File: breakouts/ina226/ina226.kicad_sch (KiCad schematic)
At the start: 14 parts, among them J1 Conn_01x01_Pin, J2 Conn_01x01_Pin, J3 Conn_01x01_Pin, J4 Conn_01x01_Pin, J5 Conn_01x01_Pin, J6 Conn_01x01_Pin, J7 Conn_01x01_Pin, J8 Conn_01x01_Pin, U1 INA226

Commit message: Feat[breakouts]: Added @TODOs
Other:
- note added: "@TODO: Add at least 1 more peripheral address config"
- note added: "@TODO: Add screw terminal for Vin+ and Vin-"
- note added: "@TODO: Assign footprints"
- note added: "@TODO: Change VS voltage"
- note added: "@TODO: Don't short the entire thing (use labels for vin+ and vin-)"
- note added: "@TODO: Fix styling (Use default symbols for voltage, ground must face ground)"
- note added: "@TODO: Remove header pins for Vin+, Vin-, A0, A1"
- note added: "@TODO: Remove series resistors"
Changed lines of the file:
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@@
-(kicad_sch (version 20230121) (generator eeschema)
+(kicad_sch (version 20230409) (generator eeschema)
   (paper "A4")
   (title_block
@@
     (fill (type none))
   )
-  (text "Chip" (at 194.31 67.31 0)
+  (text "Chip" (exclude_from_sim no)
+ (at 194.31 67.31 0)
     (effects (font (size 1.27 1.27)) (justify left bottom))
   )
-  (text "Header" (at 171.45 21.59 0)
+  (text "@TODO: Add at least 1 more peripheral address config" (exclude_from_sim no)
+    (at 23.241 97.028 0)
     (effects (font (size 1.27 1.27)) (justify left bottom))
   )
+  (text "@TODO: Remove series resistors" (exclude_from_sim no)
+ (at 23.368 82.55 0)
+    (effects (font (size 1.27 1.27)) (justify left bottom))
+  )
+  (text "@TODO: Don't short the entire thing (use labels for vin+ and vin-)" (exclude_from_sim no)
+    (at 23.241 77.597 0)
+    (effects (font (size 1.27 1.27)) (justify left bottom))
+  )
+  (text "@TODO: Remove header pins for Vin+, Vin-, A0, A1" (exclude_from_sim no)
+ (at 23.241 101.854 0)
+    (effects (font (size 1.27 1.27)) (justify left bottom))
+  )
+  (text "@TODO: Change VS voltage" (exclude_from_sim no)
+ (at 23.495 73.025 0)
+    (effects (font (size 1.27 1.27)) (justify left bottom))
+  )
+  (text "@TODO: Add screw terminal for Vin+ and Vin-\n" (exclude_from_sim no)
+ (at 23.241 87.63 0)
+    (effects (font (size 1.27 1.27)) (justify left bottom))
+  )
+  (text "Header" (exclude_from_sim no)
+ (at 171.45 21.59 0)
+    (effects (font (size 1.27 1.27)) (justify left bottom))
+  )
+  (text "@TODO: Fix styling (Use default symbols for voltage, ground must face ground)" (exclude_from_sim no)
+    (at 23.114 92.202 0)
+    (effects (font (size 1.27 1.27)) (justify left bottom))
+  )
+  (text "@TODO: Assign footprints" (exclude_from_sim no)
+ (at 22.86 107.188 0)
+    (effects (font (size 1.27 1.27)) (justify left bottom))
+  )

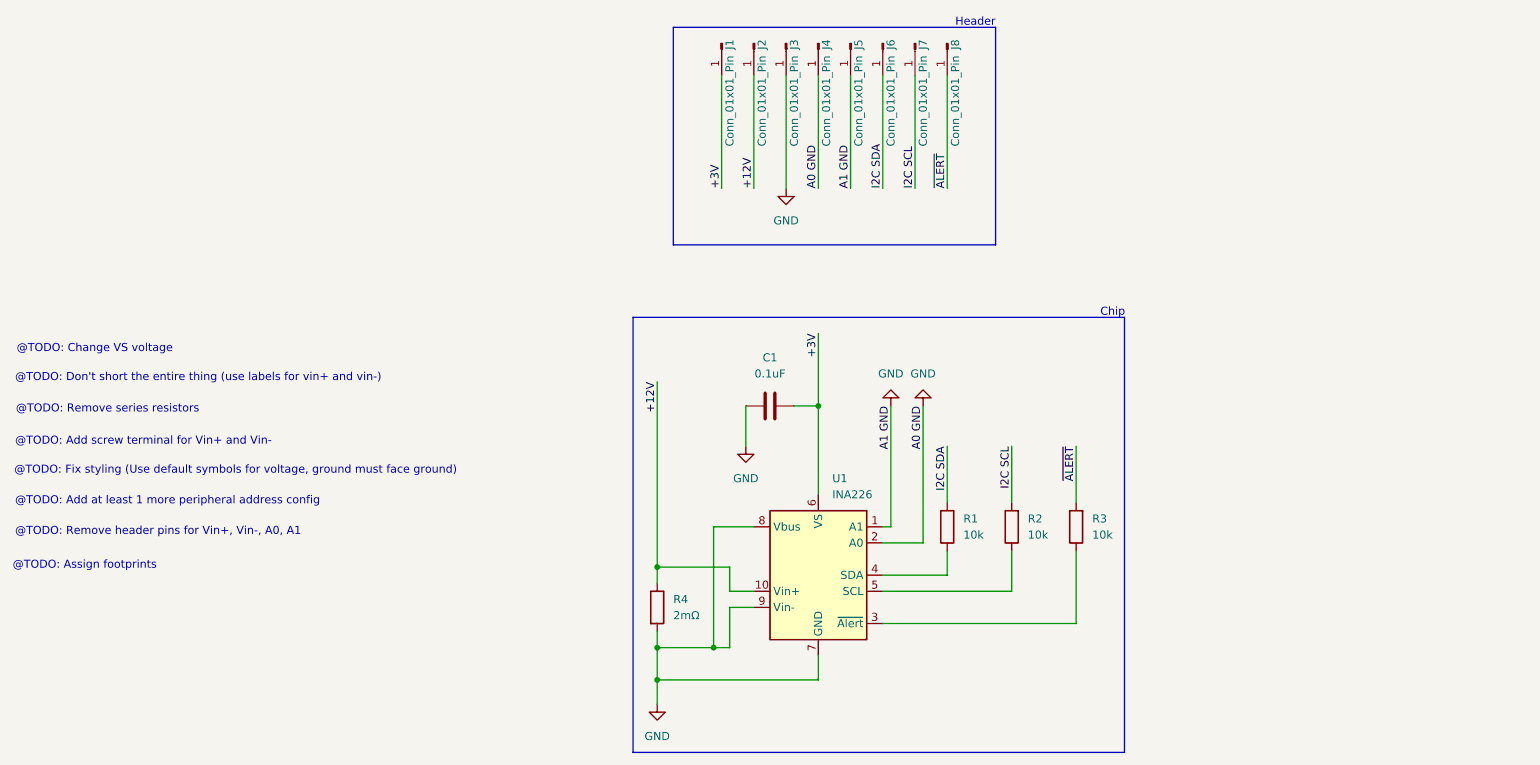
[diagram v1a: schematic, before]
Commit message: Feat[breakouts]: Fixed listed problems with ina226 breakout
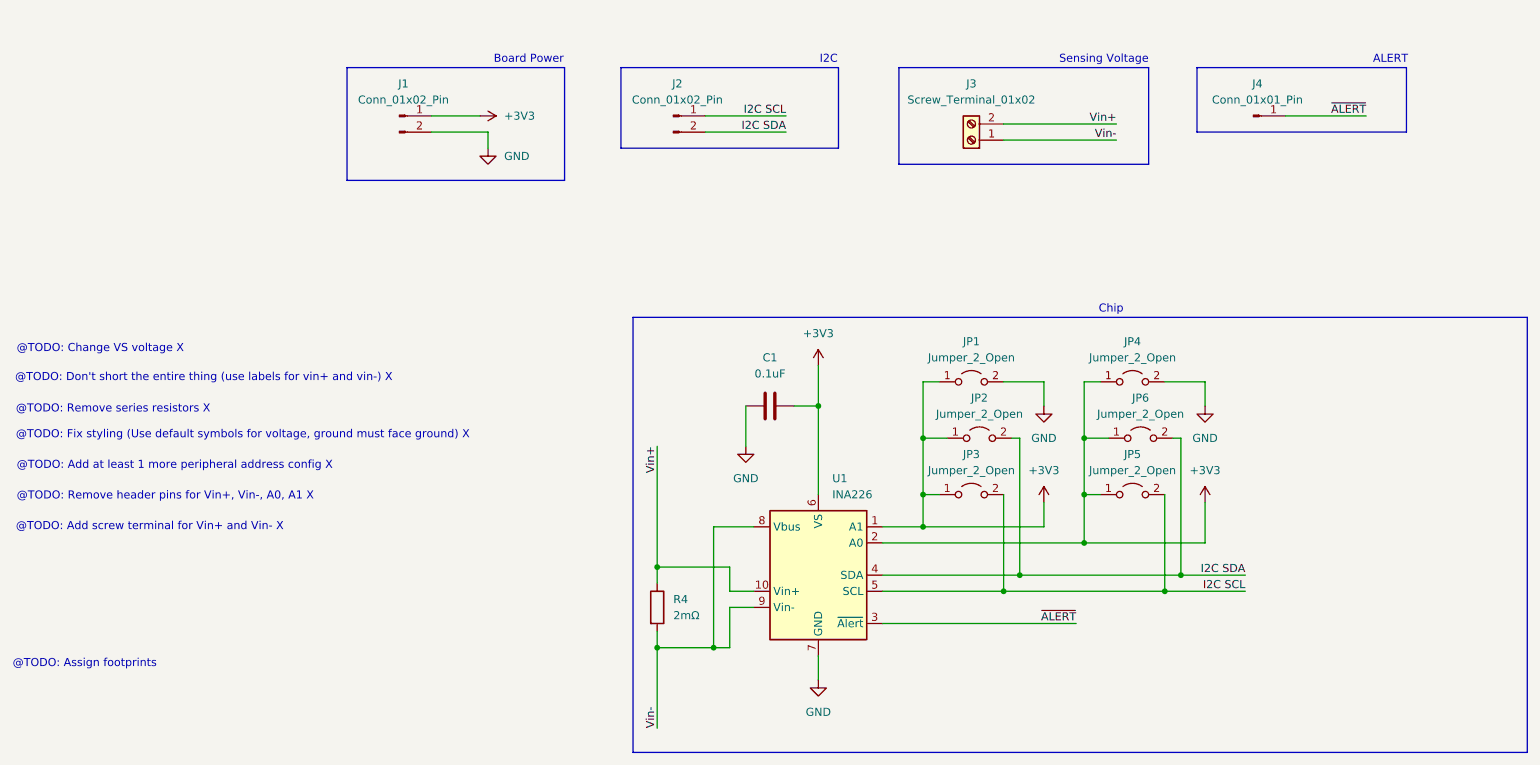
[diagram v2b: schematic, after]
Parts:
- removed J1, J2, J3, J5, J6, J7, J8: Conn_01x01_Pin, symbol Connector:Conn_01x01_Pin
- removed R1, R2, R3: 10k, symbol Device:R
- added J1, J2: Conn_01x02_Pin, symbol Connector:Conn_01x02_Pin
- added J3: Screw_Terminal_01x02, symbol Connector:Screw_Terminal_01x02
- added JP1, JP2, JP3, JP4, JP5, JP6: Jumper_2_Open, symbol Jumper:Jumper_2_Open
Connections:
- net GND: now also J1.2 (Pin_2), JP1.2 (B), JP4.2 (B); no longer J4.1 (Pin_1), R4.2, U1.1 (A1), U1.2 (A0), U1.8 (Vbus), U1.9 (Vin-)
- net I2C SCL: now also U1.5 (SCL), J2.1 (Pin_1), JP3.2 (B), JP5.2 (B)
- net I2C SDA: now also U1.4 (SDA), J2.2 (Pin_2), JP2.2 (B), JP6.2 (B)
- net ~{ALERT}: now also J4.1 (Pin_1), U1.3 (~{Alert})
- net +12V renamed Vin+
- net Vin+: now also J3.2 (Pin_2)
- net +3V renamed +3V3
- net +3V3: now also U1.1 (A1), U1.2 (A0), J1.1 (Pin_1), JP1.1 (A), JP2.1 (A), JP3.1 (A), JP4.1 (A), JP5.1 (A), JP6.1 (A)
- new net Vin-: J3.1 (Pin_1), R4.2, U1.8 (Vbus), U1.9 (Vin-)
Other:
- note added: "@TODO: Add at least 1 more peripheral address config X"
- note added: "@TODO: Add screw terminal for Vin+ and Vin- X"
- note added: "@TODO: Change VS voltage X"
- note added: "@TODO: Don't short the entire thing (use labels for vin+ and vin-) X"
- note added: "@TODO: Fix styling (Use default symbols for voltage, ground must face ground) X"
- note added: "@TODO: Remove header pins for Vin+, Vin-, A0, A1 X"
- note added: "@TODO: Remove series resistors X"
- note added: "ALERT"
- note added: "Board Power"
- note added: "I2C"
- note added: "Sensing Voltage"
- note removed: "@TODO: Add at least 1 more peripheral address config"
- note removed: "@TODO: Add screw terminal for Vin+ and Vin-"
- note removed: "@TODO: Change VS voltage"
- note removed: "@TODO: Don't short the entire thing (use labels for vin+ and vin-)"
- note removed: "@TODO: Fix styling (Use default symbols for voltage, ground must face ground)"
- note removed: "@TODO: Remove header pins for Vin+, Vin-, A0, A1"
- note removed: "@TODO: Remove series resistors"
- note removed: "Header"

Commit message: Feat[breakouts]: Separated A1/A0 from main chip schem
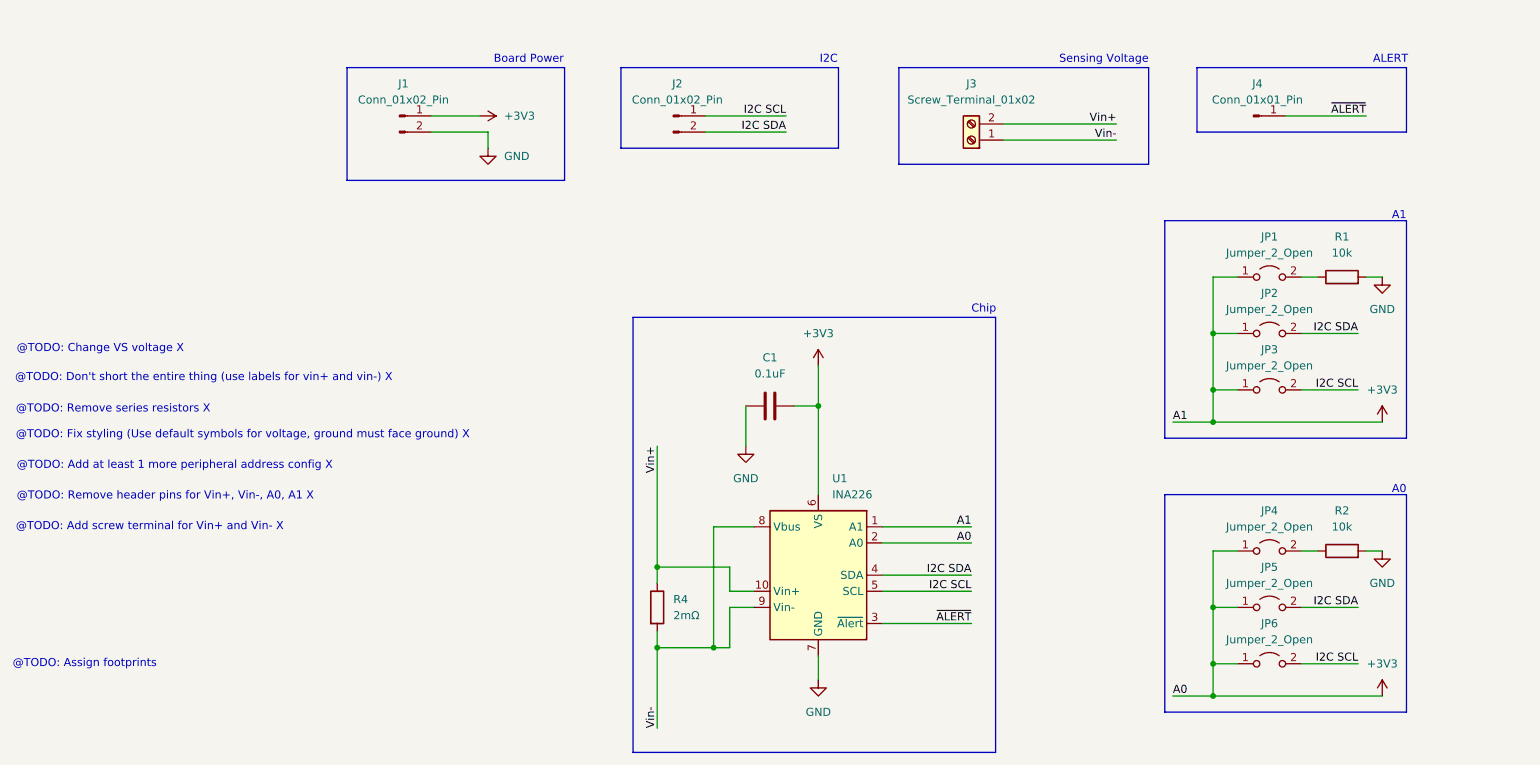
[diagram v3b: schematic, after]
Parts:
- added R1, R2: 10k, symbol Device:R
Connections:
- net GND: now also R1.2, R2.2; no longer JP1.2 (B), JP4.2 (B)
- net I2C SCL: now also JP6.2 (B); no longer JP5.2 (B)
- net I2C SDA: now also JP5.2 (B); no longer JP6.2 (B)
- new net: JP4.2 (B), R2.1
- new net: JP1.2 (B), R1.1
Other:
- note added: "A0"
- note added: "A1"

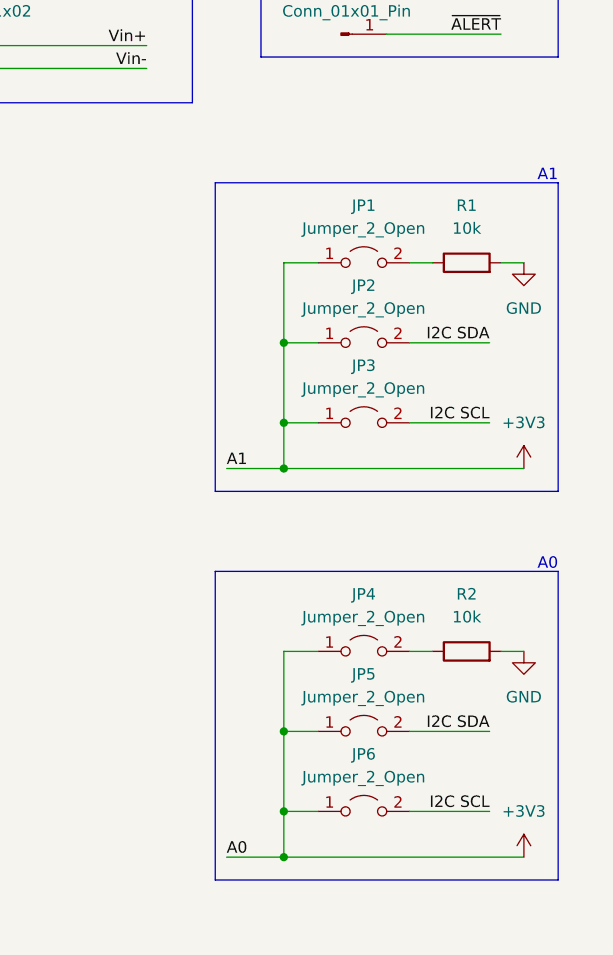
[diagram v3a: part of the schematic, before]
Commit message: Feat[breakouts]: Assigned footprints for INA226
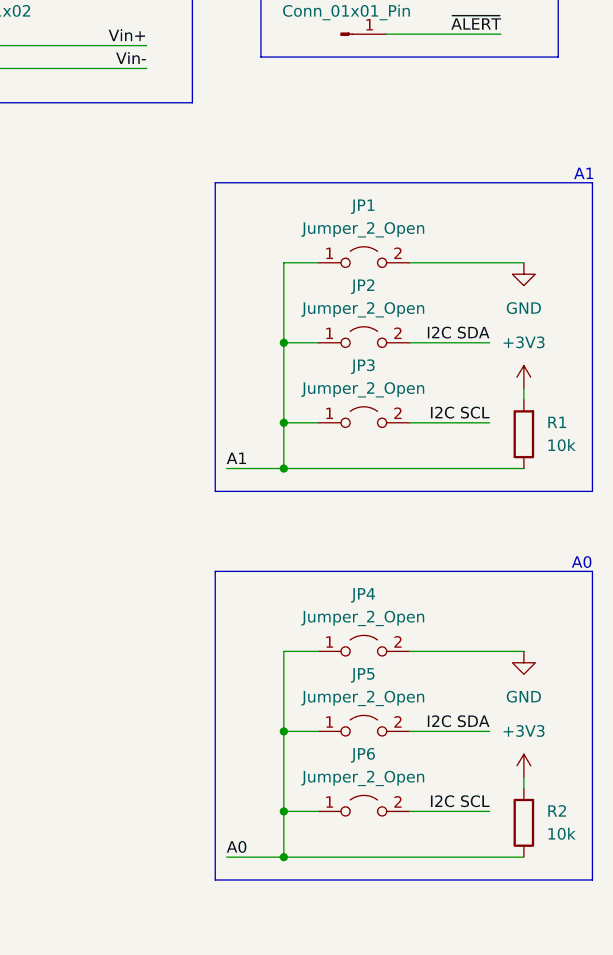
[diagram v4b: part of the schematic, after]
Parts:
- C1: footprint (none) -> Capacitor_SMD:C_0603_1608Metric
- J1, J2: footprint (none) -> Connector_PinSocket_2.54mm:PinSocket_1x02_P2.54mm_Vertical
- J3: footprint (none) -> Conn_1935776:CONN_1935776_PXC
- J4: footprint (none) -> Connector_PinSocket_2.54mm:PinSocket_1x01_P2.54mm_Vertical
- JP1, JP2, JP3, JP4, JP5, JP6: footprint (none) -> Jumper:SolderJumper-2_P1.3mm_Open_Pad1.0x1.5mm
- R1, R2, R4: footprint (none) -> Resistor_SMD:R_0603_1608Metric
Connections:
- net +3V3: now also R1.2, R2.2; no longer JP1.1 (A), JP2.1 (A), JP3.1 (A), JP4.1 (A), JP5.1 (A), JP6.1 (A), U1.1 (A1), U1.2 (A0)
- net GND: now also JP1.2 (B), JP4.2 (B); no longer R1.2, R2.2
- net A0: now reaches R2.1
- net A0: now also JP4.1 (A), JP5.1 (A), JP6.1 (A), U1.2 (A0); no longer JP4.2 (B)
- net A1: now reaches R1.1
- net A1: now also JP1.1 (A), JP2.1 (A), JP3.1 (A), U1.1 (A1); no longer JP1.2 (B)
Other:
- moved on the sheet: R1, R2

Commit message: Feat[breakouts]: Modified PCB layout, added some traces
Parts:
- R4: footprint Resistor_SMD:R_0603_1608Metric -> R_2mO_ShuntResistor:RESC6432X90N
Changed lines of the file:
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@@
       (effects (font (size 1.27 1.27)) (justify left))
     )
-    (property "Footprint" "Resistor_SMD:R_0603_1608Metric" (at 122.682 113.03 90)
+    (property "Footprint" "R_2mO_ShuntResistor:RESC6432X90N" (at 122.682 113.03 90)
       (effects (font (size 1.27 1.27)) hide)
     )

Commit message: Feat[breakouts]: Rearranged PCB layout for INA226, added ground layer
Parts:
- J1: footprint Connector_PinSocket_2.54mm:PinSocket_1x02_P2.54mm_Vertical -> Connector_PinHeader_2.54mm:PinHeader_1x02_P2.54mm_Vertical
- J4: footprint Connector_PinSocket_2.54mm:PinSocket_1x01_P2.54mm_Vertical -> Connector_PinHeader_2.54mm:PinHeader_1x01_P2.54mm_Vertical
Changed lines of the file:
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@@
       (effects (font (size 1.27 1.27)))
     )
-    (property "Footprint" "Connector_PinSocket_2.54mm:PinSocket_1x01_P2.54mm_Vertical" (at 218.44 35.56 0)
+    (property "Footprint" "Connector_PinHeader_2.54mm:PinHeader_1x01_P2.54mm_Vertical" (at 218.44 35.56 0)
       (effects (font (size 1.27 1.27)) hide)
     )
@@
       (effects (font (size 1.27 1.27)))
     )
-    (property "Footprint" "Connector_PinSocket_2.54mm:PinSocket_1x02_P2.54mm_Vertical" (at 83.82 35.56 0)
+    (property "Footprint" "Connector_PinHeader_2.54mm:PinHeader_1x02_P2.54mm_Vertical" (at 83.82 35.56 0)
       (effects (font (size 1.27 1.27)) hide)
     )

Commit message: Feat[breakouts]: Added via stitching, rearranged some components, added copper pours
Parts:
- J2: footprint Connector_PinSocket_2.54mm:PinSocket_1x02_P2.54mm_Vertical -> Connector_PinHeader_2.54mm:PinHeader_1x02_P2.54mm_Vertical
- R4: footprint R_2mO_ShuntResistor:RESC6432X90N -> Resistor_SMD:R_2512_6332Metric
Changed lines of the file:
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@@
       (effects (font (size 1.27 1.27)) (justify left))
     )
-    (property "Footprint" "R_2mO_ShuntResistor:RESC6432X90N" (at 122.682 113.03 90)
+    (property "Footprint" "Resistor_SMD:R_2512_6332Metric" (at 122.682 113.03 90)
       (effects (font (size 1.27 1.27)) hide)
     )
@@
       (effects (font (size 1.27 1.27)))
     )
-    (property "Footprint" "Connector_PinSocket_2.54mm:PinSocket_1x02_P2.54mm_Vertical" (at 127 35.56 0)
-      (effects (font (size 1.27 1.27)) hide)
-    )
+    (property "Footprint" "Connector_PinHeader_2.54mm:PinHeader_1x02_P2.54mm_Vertical" (at 127 35.56 0)
+      (effects (font (size 1.27 1.27)) hide)
+    )
